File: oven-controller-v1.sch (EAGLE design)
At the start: 21 parts, among them Q1 IRFL310, U1 ARDUINO_SHIELDLONGPADS

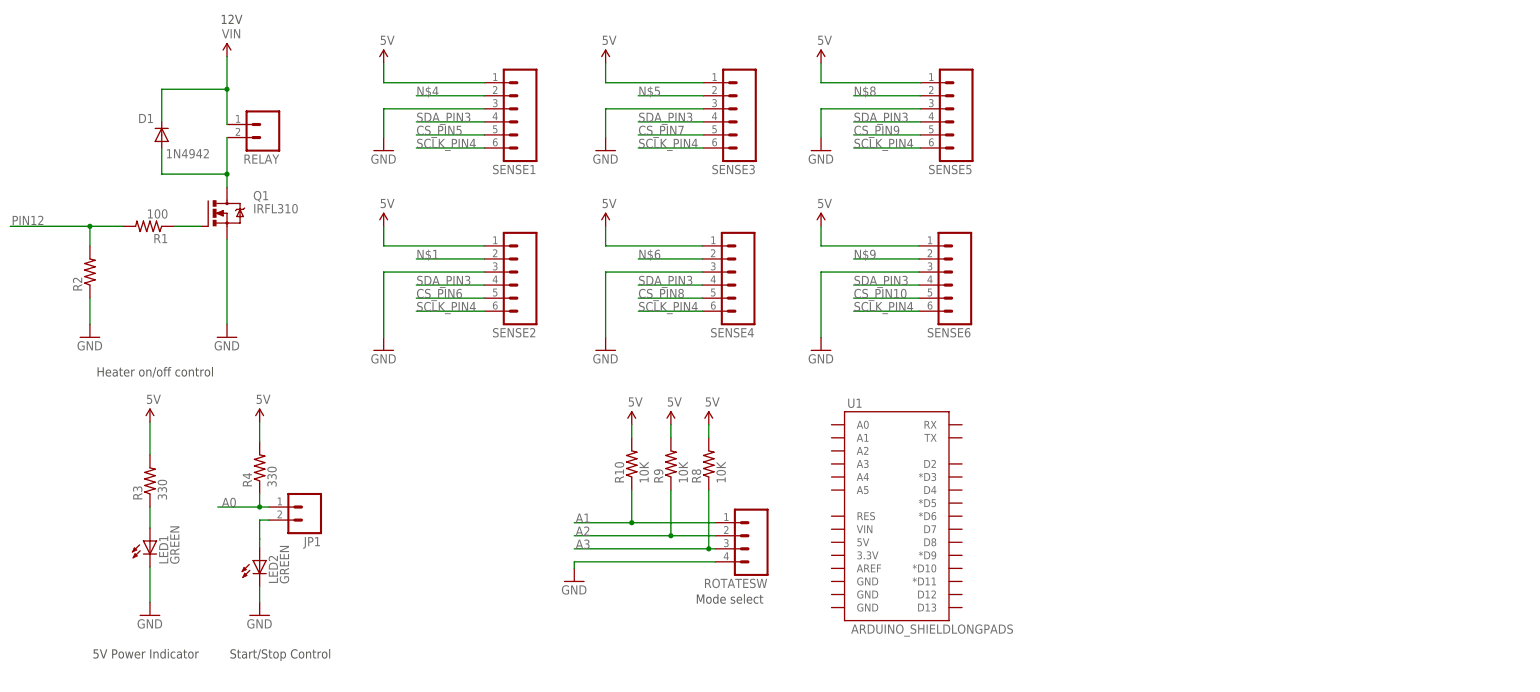
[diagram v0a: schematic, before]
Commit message: All parts on the board, cleaned up layout.
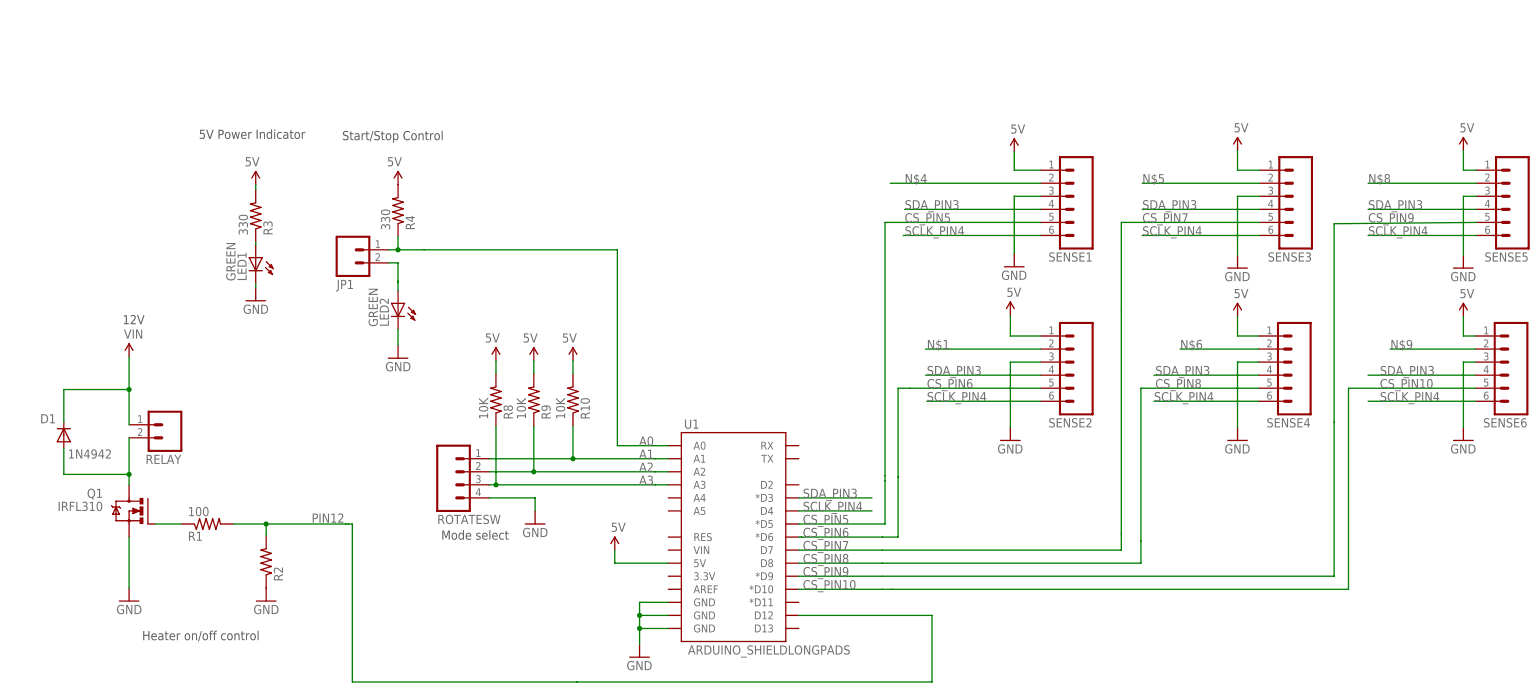
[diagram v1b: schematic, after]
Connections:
- net 5V: now also U1.5V
- net A0: now also U1.A0
- net A1: now also U1.A1
- net A2: now also U1.A2
- net A3: now also U1.A3
- net CS_PIN10: now also U1.*D10
- net CS_PIN5: now also U1.*D5
- net CS_PIN6: now also U1.*D6
- net CS_PIN7: now also U1.D7
- net CS_PIN8: now also U1.D8
- net CS_PIN9: now also U1.*D9
- net GND: now also U1.GND@0, U1.GND@1, U1.GND@2
- net PIN12: now also U1.D12
- net SCLK_PIN4: now also U1.D4
- net SDA_PIN3: now also U1.*D3
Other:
- moved on the sheet: D1, JP1, LED1, LED2, Q1, R1, R10, R2, R3, R4, R8, R9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

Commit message: Schematic and layout done. Connections to Arduino will have to be female headers because we don't have plated vias.
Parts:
- removed JP1: (no value), SparkFun-Connectors:M02LOCK_LONGPADS
- added 12VIN, START: (no value), SparkFun-Connectors:M023.5MM_LOCK
- LED2: value GREEN -> RED
- R2: value (none) -> 10k
- RELAY: device SparkFun-Connectors:M02LOCK_LONGPADS -> SparkFun-Connectors:M023.5MM_LOCK
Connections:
- removed net N$1: SENSE2.2
- removed net N$4: SENSE1.2
- removed net N$5: SENSE3.2
- removed net N$6: SENSE4.2
- removed net N$8: SENSE5.2
- removed net N$9: SENSE6.2
- net A0: now also START.1; no longer JP1.1
- net GND: now also 12VIN.2
- net N$10: now also START.2; no longer JP1.2
- net VIN: now also 12VIN.1
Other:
- moved on the sheet: D1, LED1, LED2, Q1, R1, R10, R2, R3, R4, R8, R9, RELAY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
